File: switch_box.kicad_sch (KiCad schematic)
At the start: 0 parts

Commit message: Digital IO, Relay, and Switchbox changes
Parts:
- added J5: 776280-1, 776280-1:TE_776280-1, symbol 776280-1:776280-1
- added R15, R16, R17, R18, R19, R20, R21, R22: 10K, symbol Device:R_US
- added U10, U11, U12, U9: VOM618A-3T, VOM618A-3T:SOIC254P695X242-4N, symbol VOM618A-3T:VOM618A-3T
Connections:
- net Hazards: now also R16.1, U9.4
- net Reverse: now also R20.1, U11.4
- new net: J5.6, R15.1
- new net: R15.2, U9.1
- new net: R17.2, U10.1
- new net: R19.2, U11.1
- new net: J5.5, R19.1
- new net: J5.7, R17.1
- new net: R21.2, U12.1
- new net: J5.8, R21.1
- new net +12V: J5.1
- new net +3.3V: R16.2, R18.2, R20.2, R22.2
- new net ExtraSwitch1: R18.1, U10.4
- new net ExtraSwitch2: R22.1, U12.4
- new net GND: J5.2, U10.3, U11.3, U12.3, U9.3
- new net GNDp: U10.2, U11.2, U12.2, U9.2
- new net RX: J5.3
- new net TX: J5.4

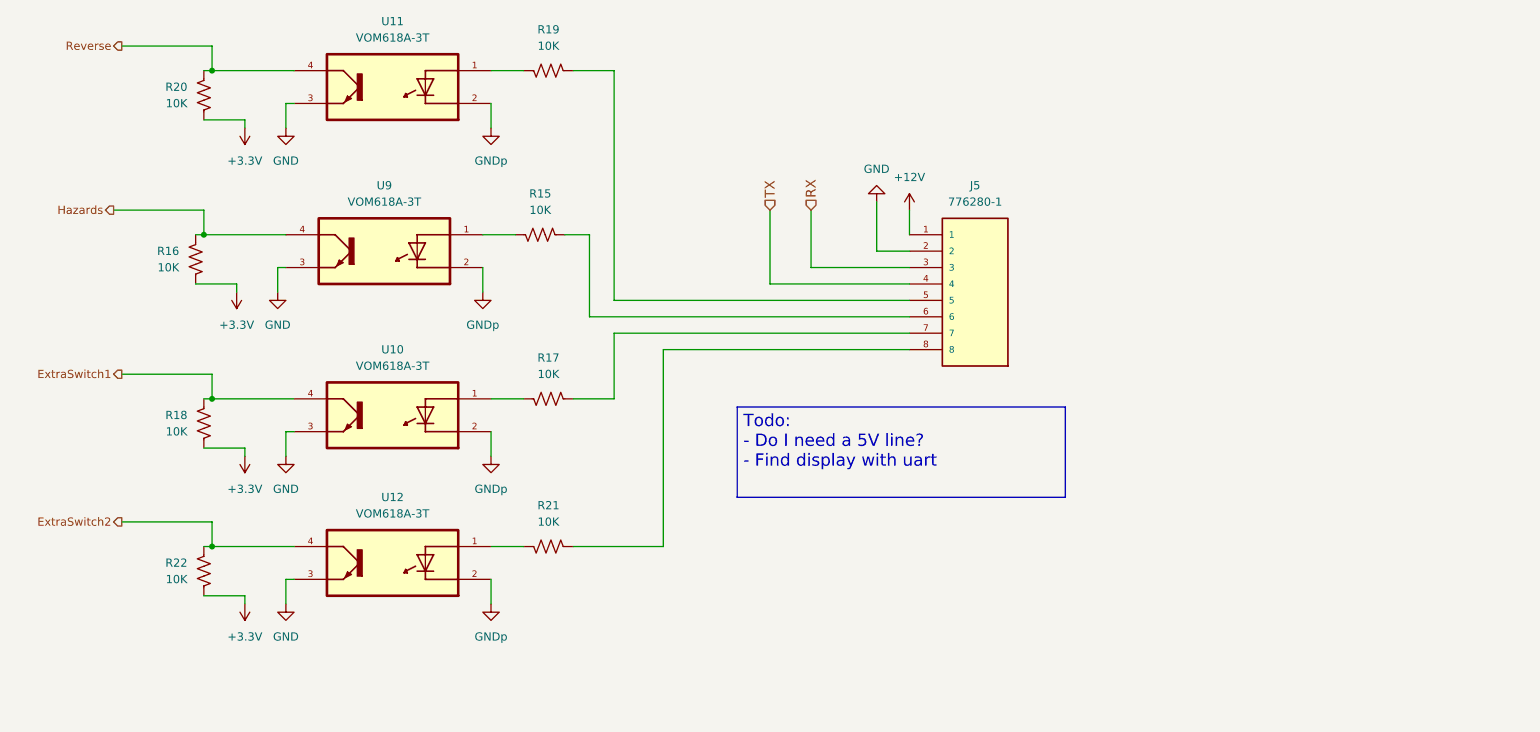
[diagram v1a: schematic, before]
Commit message: Added 5V to switchbox
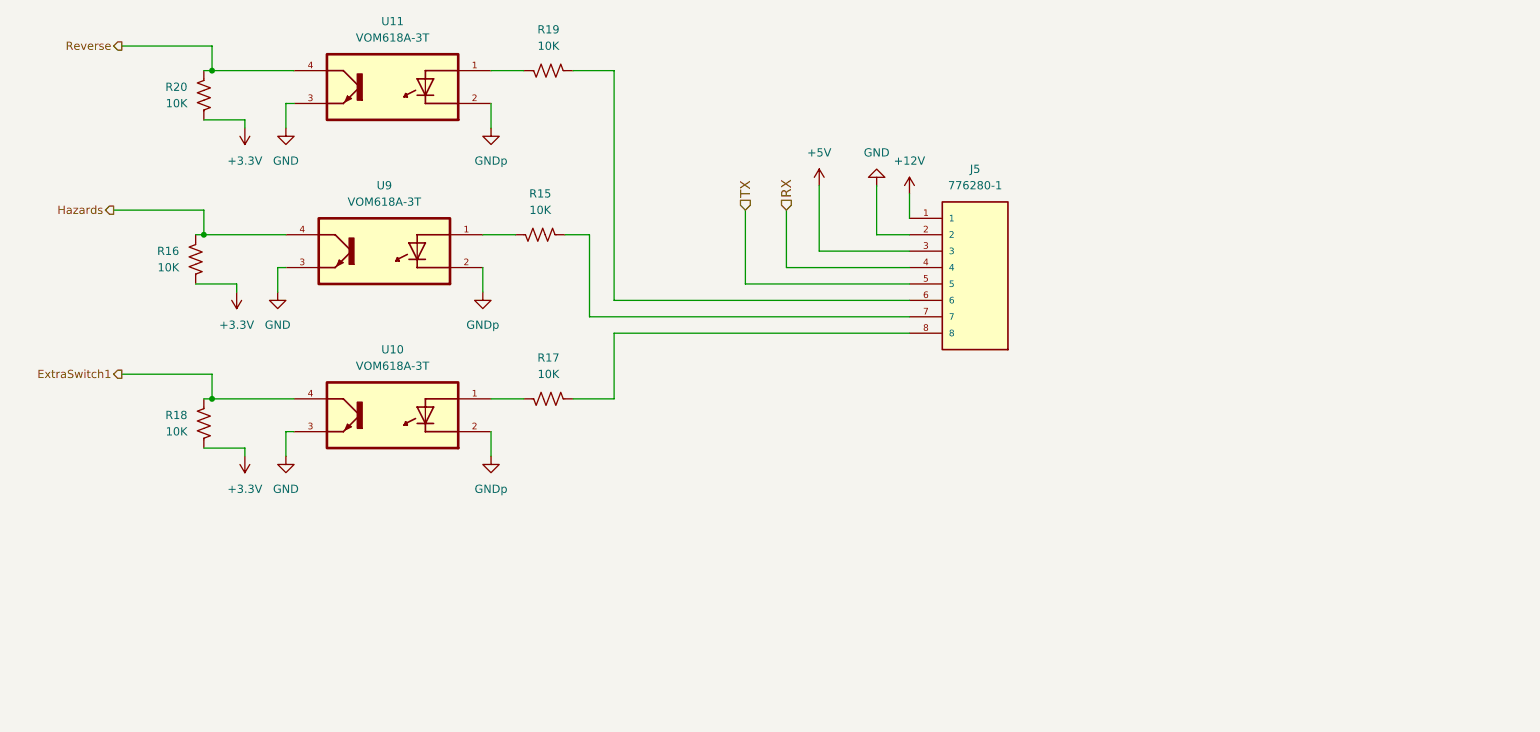
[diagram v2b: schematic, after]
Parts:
- removed R21, R22: 10K, symbol Device:R_US
- removed U12: VOM618A-3T, VOM618A-3T:SOIC254P695X242-4N, symbol VOM618A-3T:VOM618A-3T
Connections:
- net RX: now also J5.4; no longer J5.3
- net TX: now also J5.5; no longer J5.4
- net at R15.1: now also J5.7; no longer J5.6
- net at R19.1: now also J5.6; no longer J5.5
- net at R17.1: now also J5.8; no longer J5.7
- new net +5V: J5.3
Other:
- moved on the sheet: J5
